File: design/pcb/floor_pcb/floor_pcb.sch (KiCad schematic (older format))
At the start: 11 parts, among them J1 Conn_01x10_Male, J10 shock_grid, J11 shock_grid, J2 Conn_01x10_Male, J3 Conn_02x10_Top_Bottom, J4 shock_grid, J5 shock_grid, J6 shock_grid, J7 shock_grid, J8 shock_grid, J9 shock_grid

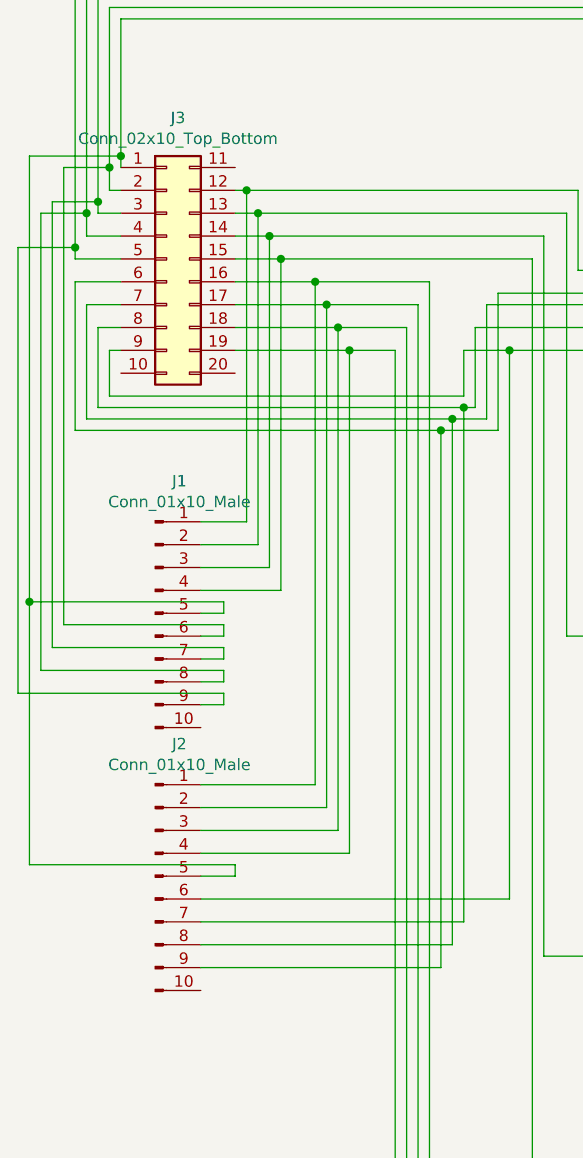
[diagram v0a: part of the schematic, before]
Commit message: Added schematic lib w/ IRL620 symbol for shield. Going to convert FET / measurement unit to hierarchical sheet. Not sure what changes were to floor_pcb.sch.
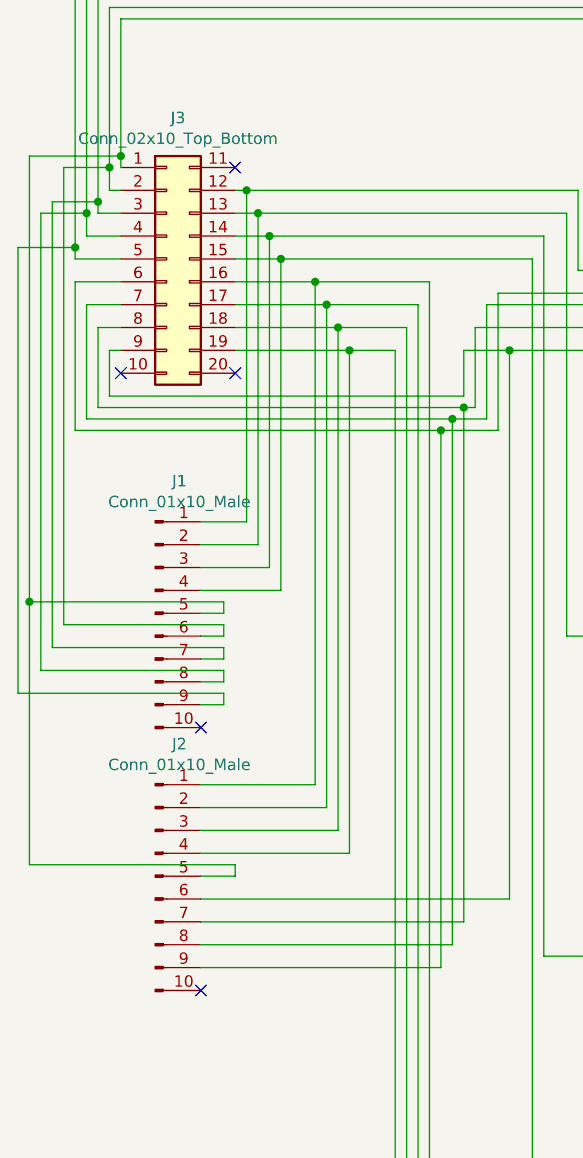
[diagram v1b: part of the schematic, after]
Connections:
- no-connect marks 0 -> 5
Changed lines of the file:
@@
 LIBS:atmel
 LIBS:contrib
-LIBS:pcb-cache
+LIBS:floor_pcb-cache
 EELAYER 26 0
 EELAYER END
@@
 Wire Wire Line
 	2350 4900 2350 2550
+NoConn ~ 1300 3850
+NoConn ~ 1300 5000
+NoConn ~ 950  2300
+NoConn ~ 1450 2300
+NoConn ~ 1450 1400
 $EndSCHEMATC

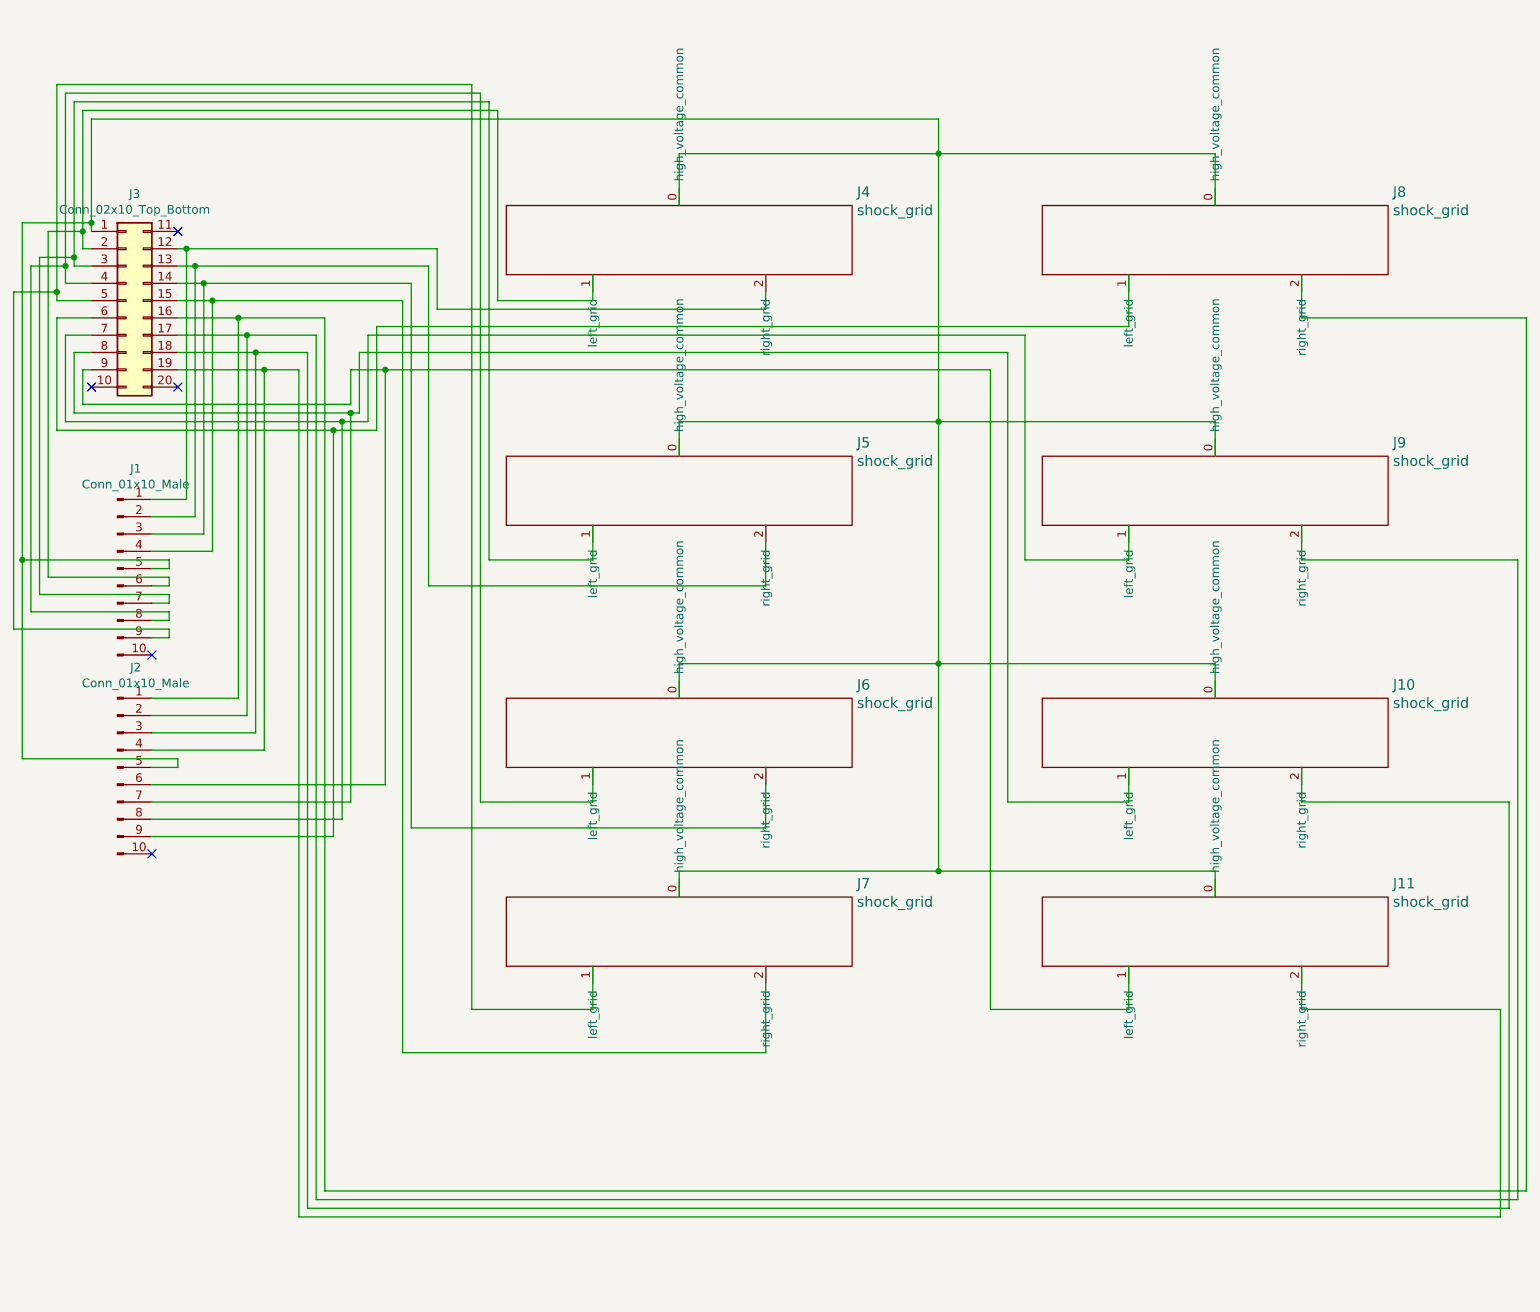
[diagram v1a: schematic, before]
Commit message: Redid some of floor PCB. Added 25pin DSub connector. Deleted old design files with one layer per file. Moved slider compressors (rails) to main file as blocks in their own layer. Added initial README explaining different lasercut design files.
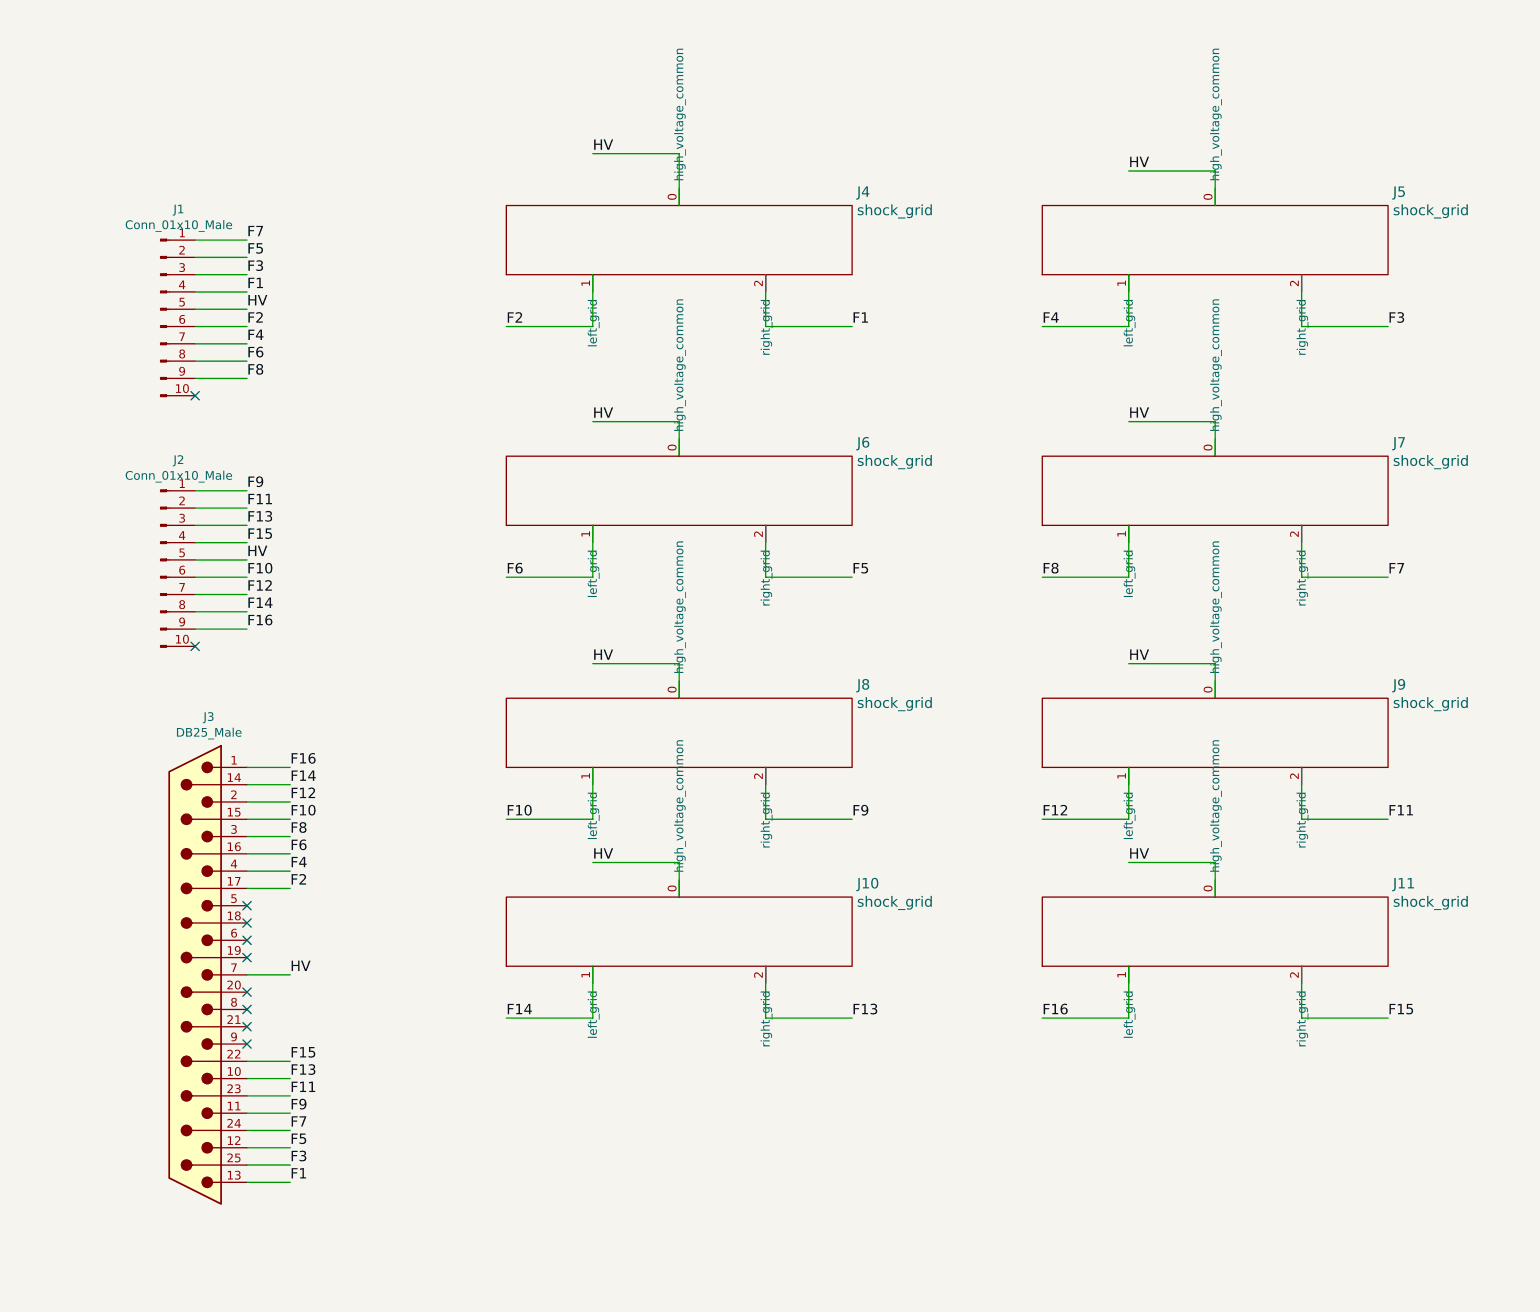
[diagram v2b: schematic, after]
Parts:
- removed J3: Conn_02x10_Top_Bottom, footprints:DIP-2x10_2.54mm_1mm_clearance, symbol Conn_02x10_Top_Bottom
- added J3: DB25_Male, Connectors_DSub:DSUB-25_Male_Horizontal_Pitch2.77x2.84mm_EdgePinOffset7.70mm_Housed_MountingHolesOffset9.12mm, symbol DB25_Male
- J10: renamed from J7; footprint footprints:electrode -> footprints:electrodes_clearance0.6mm
- J11, J4: footprint footprints:electrode -> footprints:electrodes_clearance0.6mm
- J5: renamed from J8; footprint footprints:electrode -> footprints:electrodes_clearance0.6mm
- J6: renamed from J5; footprint footprints:electrode -> footprints:electrodes_clearance0.6mm
- J7: renamed from J9; footprint footprints:electrode -> footprints:electrodes_clearance0.6mm
- J8: renamed from J6; footprint footprints:electrode -> footprints:electrodes_clearance0.6mm
- J9: renamed from J10; footprint footprints:electrode -> footprints:electrodes_clearance0.6mm
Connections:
- net HV: now reaches J1.5 (Pin_5), J10.0 (high_voltage_common), J11.0 (high_voltage_common), J2.5 (Pin_5), J4.0 (high_voltage_common), J5.0 (high_voltage_common), J6.0 (high_voltage_common), J7.0 (high_voltage_common), J8.0 (high_voltage_common), J9.0 (high_voltage_common)
- net HV: now also J3.7
- net F1: now reaches J4.2 (right_grid)
- net F1: now also J1.4 (Pin_4), J3.13; no longer J1.1 (Pin_1)
- net F5: now reaches J1.2 (Pin_2), J6.2 (right_grid)
- net F5: now also J3.12
- net F3: now reaches J1.3 (Pin_3)
- net F3: now also J5.2 (right_grid), J3.25 (P25); no longer J8.2 (right_grid)
- net F13: now reaches J10.2 (right_grid)
- net F13: now also J2.3 (Pin_3), J3.10; no longer J1.4 (Pin_4)
- net F9: now reaches J2.1 (Pin_1)
- net F9: now also J8.2 (right_grid), J3.11; no longer J5.2 (right_grid)
- net F11: now reaches J2.2 (Pin_2)
- net F11: now also J9.2 (right_grid), J3.23 (P23); no longer J7.2 (right_grid)
- net F15: now reaches J11.2 (right_grid), J2.4 (Pin_4)
- net F15: now also J3.22 (P22)
- net F2: now reaches J1.6 (Pin_6), J4.1 (left_grid)
- net F2: now also J3.17 (P17)
- net F4: now reaches J1.7 (Pin_7)
- net F4: now also J5.1 (left_grid), J3.4; no longer J6.1 (left_grid)
- net F10: now reaches J8.1 (left_grid)
- net F10: now also J2.6 (Pin_6), J3.15 (P15); no longer J1.8 (Pin_8)
- net F14: now reaches J10.1 (left_grid)
- net F14: now also J2.8 (Pin_8), J3.14 (P14); no longer J1.9 (Pin_9)
- net F16: now reaches J2.9 (Pin_9)
- net F16: now also J11.1 (left_grid), J3.1; no longer J5.1 (left_grid)
- net F8: now reaches J7.1 (left_grid)
- net F8: now also J1.9 (Pin_9), J3.3; no longer J2.8 (Pin_8)
- net F12: now reaches J2.7 (Pin_7), J9.1 (left_grid)
- net F12: now also J3.2
- new net F6: J1.8 (Pin_8), J3.16 (P16), J6.1 (left_grid)
- new net F7: J1.1 (Pin_1), J3.24 (P24), J7.2 (right_grid)
- no-connect marks 5 -> 10
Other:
- moved on the sheet: J1, J2

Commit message: Fixed bug I made in electrode vertices. Ceiling pcb pretty much done. Need to name F<N> nets consistently across Kicad projects.
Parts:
- J10, J11, J4, J5, J6, J7, J8, J9: footprint footprints:electrodes_clearance0.6mm -> footprints:electrodes_clearance0.6mm_W0.4mm_centerflush
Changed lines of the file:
@@
 F 0 "J4" H 5378 1728 60  0000 L CNN
 F 1 "shock_grid" H 5378 1622 60  0000 L CNN
-F 2 "footprints:electrodes_clearance0.6mm" H 4350 1450 60  0001 C CNN
+F 2 "footprints:electrodes_clearance0.6mm_W0.4mm_centerflush" H 4350 1450 60  0001 C CNN
 F 3 "" H 4350 1450 60  0001 C CNN
 	1    4350 1450
@@
 F 0 "J6" H 5378 3178 60  0000 L CNN
 F 1 "shock_grid" H 5378 3072 60  0000 L CNN
-F 2 "footprints:electrodes_clearance0.6mm" H 4350 2900 60  0001 C CNN
+F 2 "footprints:electrodes_clearance0.6mm_W0.4mm_centerflush" H 4350 2900 60  0001 C CNN
 F 3 "" H 4350 2900 60  0001 C CNN
 	1    4350 2900
@@
 F 0 "J5" H 8478 1728 60  0000 L CNN
 F 1 "shock_grid" H 8478 1622 60  0000 L CNN
-F 2 "footprints:electrodes_clearance0.6mm" H 7450 1450 60  0001 C CNN
+F 2 "footprints:electrodes_clearance0.6mm_W0.4mm_centerflush" H 7450 1450 60  0001 C CNN
 F 3 "" H 7450 1450 60  0001 C CNN
 	1    7450 1450
@@
 F 0 "J7" H 8478 3178 60  0000 L CNN
 F 1 "shock_grid" H 8478 3072 60  0000 L CNN
-F 2 "footprints:electrodes_clearance0.6mm" H 7450 2900 60  0001 C CNN
+F 2 "footprints:electrodes_clearance0.6mm_W0.4mm_centerflush" H 7450 2900 60  0001 C CNN
 F 3 "" H 7450 2900 60  0001 C CNN
 	1    7450 2900
@@
 F 0 "J8" H 5378 4578 60  0000 L CNN
 F 1 "shock_grid" H 5378 4472 60  0000 L CNN
-F 2 "footprints:electrodes_clearance0.6mm" H 4350 4300 60  0001 C CNN
+F 2 "footprints:electrodes_clearance0.6mm_W0.4mm_centerflush" H 4350 4300 60  0001 C CNN
 F 3 "" H 4350 4300 60  0001 C CNN
 	1    4350 4300
@@
 F 0 "J9" H 8478 4578 60  0000 L CNN
 F 1 "shock_grid" H 8478 4472 60  0000 L CNN
-F 2 "footprints:electrodes_clearance0.6mm" H 7450 4300 60  0001 C CNN
+F 2 "footprints:electrodes_clearance0.6mm_W0.4mm_centerflush" H 7450 4300 60  0001 C CNN
 F 3 "" H 7450 4300 60  0001 C CNN
 	1    7450 4300
@@
 F 0 "J10" H 5378 5728 60  0000 L CNN
 F 1 "shock_grid" H 5378 5622 60  0000 L CNN
-F 2 "footprints:electrodes_clearance0.6mm" H 4350 5450 60  0001 C CNN
+F 2 "footprints:electrodes_clearance0.6mm_W0.4mm_centerflush" H 4350 5450 60  0001 C CNN
 F 3 "" H 4350 5450 60  0001 C CNN
 	1    4350 5450
@@
 F 0 "J11" H 8478 5728 60  0000 L CNN
 F 1 "shock_grid" H 8478 5622 60  0000 L CNN
-F 2 "footprints:electrodes_clearance0.6mm" H 7450 5450 60  0001 C CNN
+F 2 "footprints:electrodes_clearance0.6mm_W0.4mm_centerflush" H 7450 5450 60  0001 C CNN
 F 3 "" H 7450 5450 60  0001 C CNN
 	1    7450 5450
